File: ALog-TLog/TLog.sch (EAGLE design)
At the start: 98 parts, among them IC1 ATMEGA644M, J6 5.5x2.1mm Barrel, Q5 MOSFET_PCH-IRLML2244, Q6 MOSFET_PCH-IRLML2244, Q7 MOSFET_PCH-IRLML2244, Q8 MOSFET-NCH-BSS138, Q9 MOSFET-NCH-BSS138, U2 FT231X-Q, U3 915MHz, U4 SX1509, X2 87832-14

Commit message: Updated Gerber
Made changes to silk screen on universal header and updated gerber files
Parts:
- X2: device con-molex:87832-14 -> bschulz:87832-14
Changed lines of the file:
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@@
 <attribute name="MPN" value="RC0603FR-07330RL"/>
 </part>
-<part name="X2" library="con-molex" library_urn="urn:adsk.eagle:library:165" deviceset="87832-14" device="">
+<part name="X2" library="bschulz" deviceset="87832-14" device="">
 <attribute name="DIGIKEY" value="WM18702-ND"/>
 <attribute name="MF" value="Molex"/>

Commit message: Minor changes, updated gerber (presumptive final)
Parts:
- U$1: value CRYSTALTXC_8MHZ -> CRYSTAL_5X3.2_2LEAD; device bschulz:CRYSTALTXC_8MHZ -> bschulz:CRYSTAL_5X3.2_2LEAD
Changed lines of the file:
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@@
 <?xml version="1.0" encoding="utf-8"?>
 <!DOCTYPE eagle SYSTEM "eagle.dtd">
-<eagle version="8.5.1">
+<eagle version="8.3.2">
 <drawing>
 <settings>
@@
 <grid distance="0.1" unitdist="inch" unit="inch" style="lines" multiple="1" display="no" altdistance="0.01" altunitdist="inch" altunit="inch"/>
 <layers>
-<layer number="1" name="Top" color="4" fill="1" visible="yes" active="no"/>
-<layer number="2" name="Route2" color="1" fill="3" visible="yes" active="no"/>
-<layer number="3" name="Route3" color="4" fill="3" visible="yes" active="no"/>
-<layer number="4" name="Route4" color="1" fill="4" visible="yes" active="no"/>
-<layer number="5" name="Route5" color="4" fill="4" visible="yes" active="no"/>
-<layer number="6" name="Route6" color="1" fill="8" visible="yes" active="no"/>
-<layer number="7" name="Route7" color="4" fill="8" visible="yes" active="no"/>
-<layer number="8" name="Route8" color="1" fill="2" visible="yes" active="no"/>
-<layer number="9" name="Route9" color="4" fill="2" visible="yes" active="no"/>
-<layer number="10" name="Route10" color="1" fill="7" visible="yes" active="no"/>
-<layer number="11" name="Route11" color="4" fill="7" visible="yes" active="no"/>
-<layer number="12" name="Route12" color="1" fill="5" visible="yes" active="no"/>
-<layer number="13" name="Route13" color="4" fill="5" visible="yes" active="no"/>
-<layer number="14" name="Route14" color="1" fill="6" visible="yes" active="no"/>
-<layer number="15" name="Route15" color="4" fill="6" visible="yes" active="no"/>
-<layer number="16" name="Bottom" color="1" fill="1" visible="yes" active="no"/>
-<layer number="17" name="Pads" color="2" fill="1" visible="yes" active="no"/>
-<layer number="18" name="Vias" color="2" fill="1" visible="yes" active="no"/>
-<layer number="19" name="Unrouted" color="6" fill="1" visible="yes" active="no"/>
-<layer number="20" name="Dimension" color="15" fill="1" visible="yes" active="no"/>
-<layer number="21" name="tPlace" color="7" fill="1" visible="yes" active="no"/>
-<layer number="22" name="bPlace" color="7" fill="1" visible="yes" active="no"/>
-<layer number="23" name="tOrigins" color="15" fill="1" visible="yes" active="no"/>
-<layer number="24" name="bOrigins" color="15" fill="1" visible="yes" active="no"/>
-<layer number="25" name="tNames" color="7" fill="1" visible="yes" active="no"/>
-<layer number="26" name="bNames" color="7" fill="1" visible="yes" active="no"/>
-<layer number="27" name="tValues" color="7" fill="1" visible="yes" active="no"/>
-<layer number="28" name="bValues" color="7" fill="1" visible="yes" active="no"/>
+<layer number="1" name="Top" color="4" fill="1" visible="no" active="no"/>
+<layer number="2" name="Route2" color="1" fill="3" visible="no" active="no"/>
+<layer number="3" name="Route3" color="4" fill="3" visible="no" active="no"/>
+<layer number="4" name="Route4" color="1" fill="4" visible="no" active="no"/>
+<layer number="5" name="Route5" color="4" fill="4" visible="no" active="no"/>
+<layer number="6" name="Route6" color="1" fill="8" visible="no" active="no"/>
+<layer number="7" name="Route7" color="4" fill="8" visible="no" active="no"/>
+<layer number="8" name="Route8" color="1" fill="2" visible="no" active="no"/>
+<layer number="9" name="Route9" color="4" fill="2" visible="no" active="no"/>
+<layer number="10" name="Route10" color="1" fill="7" visible="no" active="no"/>
+<layer number="11" name="Route11" color="4" fill="7" visible="no" active="no"/>
+<layer number="12" name="Route12" color="1" fill="5" visible="no" active="no"/>
+<layer number="13" name="Route13" color="4" fill="5" visible="no" active="no"/>
+<layer number="14" name="Route14" color="1" fill="6" visible="no" active="no"/>
+<layer number="15" name="Route15" color="4" fill="6" visible="no" active="no"/>
+<layer number="16" name="Bottom" color="1" fill="1" visible="no" active="no"/>
+<layer number="17" name="Pads" color="2" fill="1" visible="no" active="no"/>
+<layer number="18" name="Vias" color="2" fill="1" visible="no" active="no"/>
+<layer number="19" name="Unrouted" color="6" fill="1" visible="no" active="no"/>
+<layer number="20" name="Dimension" color="15" fill="1" visible="no" active="no"/>
+<layer number="21" name="tPlace" color="7" fill="1" visible="no" active="no"/>
+<layer number="22" name="bPlace" color="7" fill="1" visible="no" active="no"/>
+<layer number="23" name="tOrigins" color="15" fill="1" visible="no" active="no"/>
+<layer number="24" name="bOrigins" color="15" fill="1" visible="no" active="no"/>
+<layer number="25" name="tNames" color="7" fill="1" visible="no" active="no"/>
+<layer number="26" name="bNames" color="7" fill="1" visible="no" active="no"/>
+<layer number="27" name="tValues" color="7" fill="1" visible="no" active="no"/>
+<layer number="28" name="bValues" color="7" fill="1" visible="no" active="no"/>
 <layer number="29" name="tStop" color="7" fill="3" visible="no" active="no"/>
 <layer number="30" name="bStop" color="7" fill="6" visible="no" active="no"/>
@@
 <layer number="35" name="tGlue" color="7" fill="4" visible="no" active="no"/>
 <layer number="36" name="bGlue" color="7" fill="5" visible="no" active="no"/>
-<layer number="37" name="tTest" color="7" fill="1" visible="yes" active="no"/>
-<layer number="38" name="bTest" color="7" fill="1" visible="yes" active="no"/>
+<layer number="37" name="tTest" color="7" fill="1" visible="no" active="no"/>
+<layer number="38" name="bTest" color="7" fill="1" visible="no" active="no"/>
 <layer number="39" name="tKeepout" color="4" fill="11" visible="no" active="no"/>
 <layer number="40" name="bKeepout" color="1" fill="11" visible="no" active="no"/>
@@
 <layer number="44" name="Drills" color="7" fill="1" visible="no" active="no"/>
 <layer number="45" name="Holes" color="7" fill="1" visible="no" active="no"/>
-<layer number="46" name="Milling" color="3" fill="1" visible="yes" active="no"/>
-<layer number="47" name="Measures" color="7" fill="1" visible="yes" active="no"/>
-<layer number="48" name="Document" color="7" fill="1" visible="yes" active="no"/>
-<layer number="49" name="Reference" color="7" fill="1" visible="yes" active="no"/>
-<layer number="50" name="dxf" color="7" fill="1" visible="yes" active="no"/>
-<layer number="51" name="tDocu" color="7" fill="1" visible="yes" active="no"/>
-<layer number="52" name="bDocu" color="7" fill="1" visible="yes" active="no"/>
-<layer number="53" name="tGND_GNDA" color="7" fill="9" visible="yes" active="no"/>
-<layer number="54" name="bGND_GNDA" color="1" fill="9" visible="yes" active="no"/>
-<layer number="56" name="wert" color="7" fill="1" visible="yes" active="no"/>
-<layer number="57" name="tCAD" color="7" fill="1" visible="yes" active="no"/>
-<layer number="59" name="tCarbon" color="7" fill="1" visible="yes" active="no"/>
-<layer number="60" name="bCarbon" color="7" fill="1" visible="yes" active="no"/>
+<layer number="46" name="Milling" color="3" fill="1" visible="no" active="no"/>
+<layer number="47" name="Measures" color="7" fill="1" visible="no" active="no"/>
+<layer number="48" name="Document" color="7" fill="1" visible="no" active="no"/>
+<layer number="49" name="Reference" color="7" fill="1" visible="no" active="no"/>
+<layer number="50" name="dxf" color="7" fill="1" visible="no" active="no"/>
+<layer number="51" name="tDocu" color="7" fill="1" visible="no" active="no"/>
+<layer number="52" name="bDocu" color="7" fill="1" visible="no" active="no"/>
+<layer number="53" name="tGND_GNDA" color="7" fill="9" visible="no" active="no"/>
+<layer number="54" name="bGND_GNDA" color="1" fill="9" visible="no" active="no"/>
+<layer number="56" name="wert" color="7" fill="1" visible="no" active="no"/>
+<layer number="57" name="tCAD" color="7" fill="1" visible="no" active="no"/>
+<layer number="59" name="tCarbon" color="7" fill="1" visible="no" active="no"/>
+<layer number="60" name="bCarbon" color="7" fill="1" visible="no" active="no"/>
 <layer number="90" name="Modules" color="5" fill="1" visible="yes" active="yes"/>
 <layer number="91" name="Nets" color="2" fill="1" visible="yes" active="yes"/>
@@
 <part name="U3" library="SparkFun-RF" library_urn="urn:adsk.eagle:library:531" deviceset="RFM69H" device="CW-915" value="915MHz"/>
 <part name="X1" library="bschulz" deviceset="SMA" device="_EDGE"/>
-<part name="R16" library="rcl" deviceset="R-EU_" device="R0603" value="FB">
+<part name="R16" library="rcl" library_urn="urn:adsk.eagle:library:334" deviceset="R-EU_" device="R0603" package3d_urn="urn:adsk.eagle:package:23555/2" value="FB">
 <attribute name="DIGIKEY" value="1276-6358-1-ND"/>
 <attribute name="MF" value="Samsung"/>
 <attribute name="MPN" value="CIC10P471NC"/>
 </part>
-<part name="R17" library="rcl" deviceset="R-EU_" device="R0603" value="FB">
+<part name="R17" library="rcl" library_urn="urn:adsk.eagle:library:334" deviceset="R-EU_" device="R0603" package3d_urn="urn:adsk.eagle:package:23555/2" value="FB">
 <attribute name="DIGIKEY" value="1276-6358-1-ND"/>
 <attribute name="MF" value="Samsung"/>
@@
 <part name="SUPPLY47" library="supply2" library_urn="urn:adsk.eagle:library:372" deviceset="GND" device=""/>
 <part name="MICRO_USB" library="bschulz" deviceset="MICRO_USB_LONGPADS" device=""/>
-<part name="U$1" library="bschulz" deviceset="CRYSTAL" device="TXC_8MHZ"/>
+<part name="U$1" library="bschulz" deviceset="CRYSTAL_5X3.2_2LEAD" device=""/>
 <part name="R4" library="bschulz" deviceset="R-EU_" device="R0603" technology="330" value="330">
 <attribute name="MPN" value="RC0603FR-07330RL"/>
@@
 will not be understood (or retained) with this version.
 </note>
+<note version="8.3" severity="warning">
+Since Version 8.3, EAGLE supports the association of 3D packages
+with devices in libraries, schematics, and board files. Those 3D
+packages will not be understood (or retained) with this version.
+</note>
 </compatibility>

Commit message: Presumptive Final gerbers for TLog Mrk 1.1
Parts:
- ISP2: device adafruit:AVRISP-6 -> bschulz:AVRISP-6
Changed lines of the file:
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@@
 <?xml version="1.0" encoding="utf-8"?>
 <!DOCTYPE eagle SYSTEM "eagle.dtd">
-<eagle version="8.3.2">
+<eagle version="8.5.1">
 <drawing>
 <settings>
@@
 <attribute name="MPN" value="OSTTE100104"/>
 </part>
-<part name="ISP2" library="adafruit" library_urn="urn:adsk.eagle:library:420" deviceset="AVRISP" device="-6">
+<part name="ISP2" library="bschulz" deviceset="AVRISP" device="-6">
 <attribute name="DIGIKEY" value="609-3234-ND"/>
 <attribute name="MF" value="Amphenol"/>

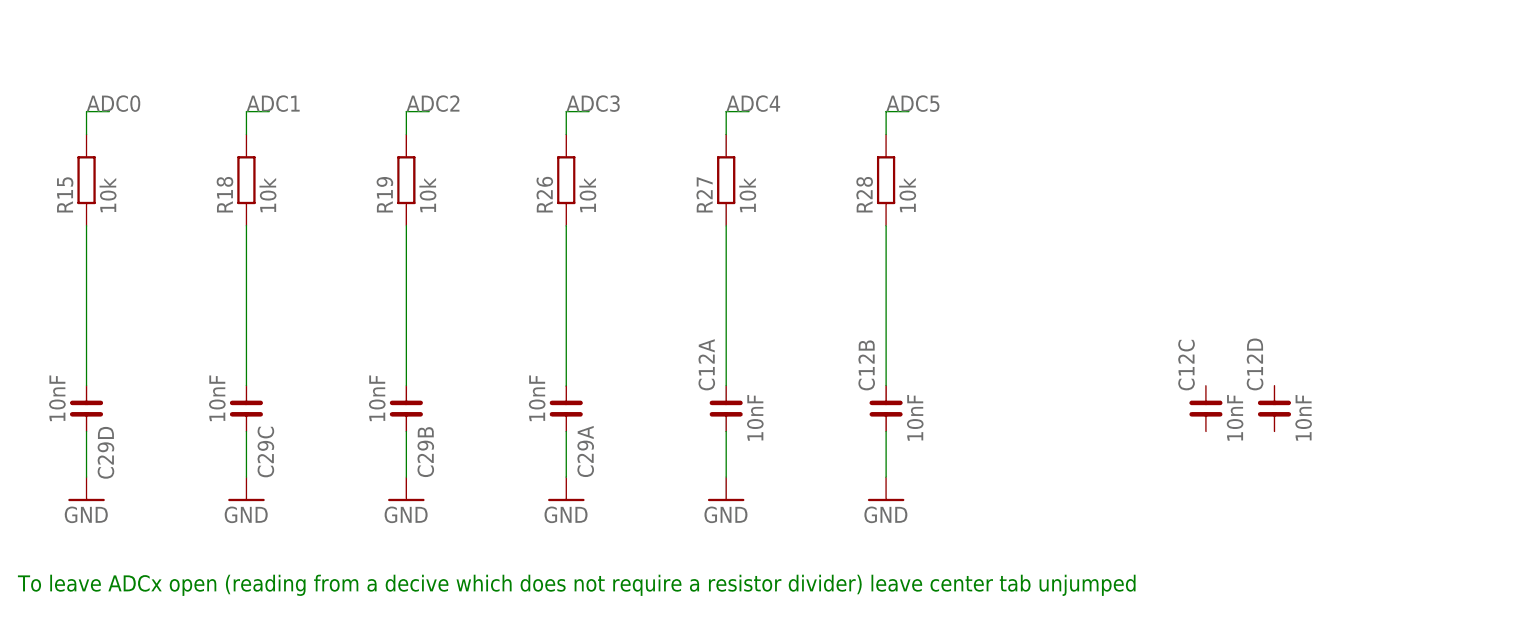
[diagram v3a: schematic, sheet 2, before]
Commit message: Issue Fix
Patial fix of issues: #12, #9, #8 (fixed in schematic, but not fully routed)
Full fix of issues: #10, #7
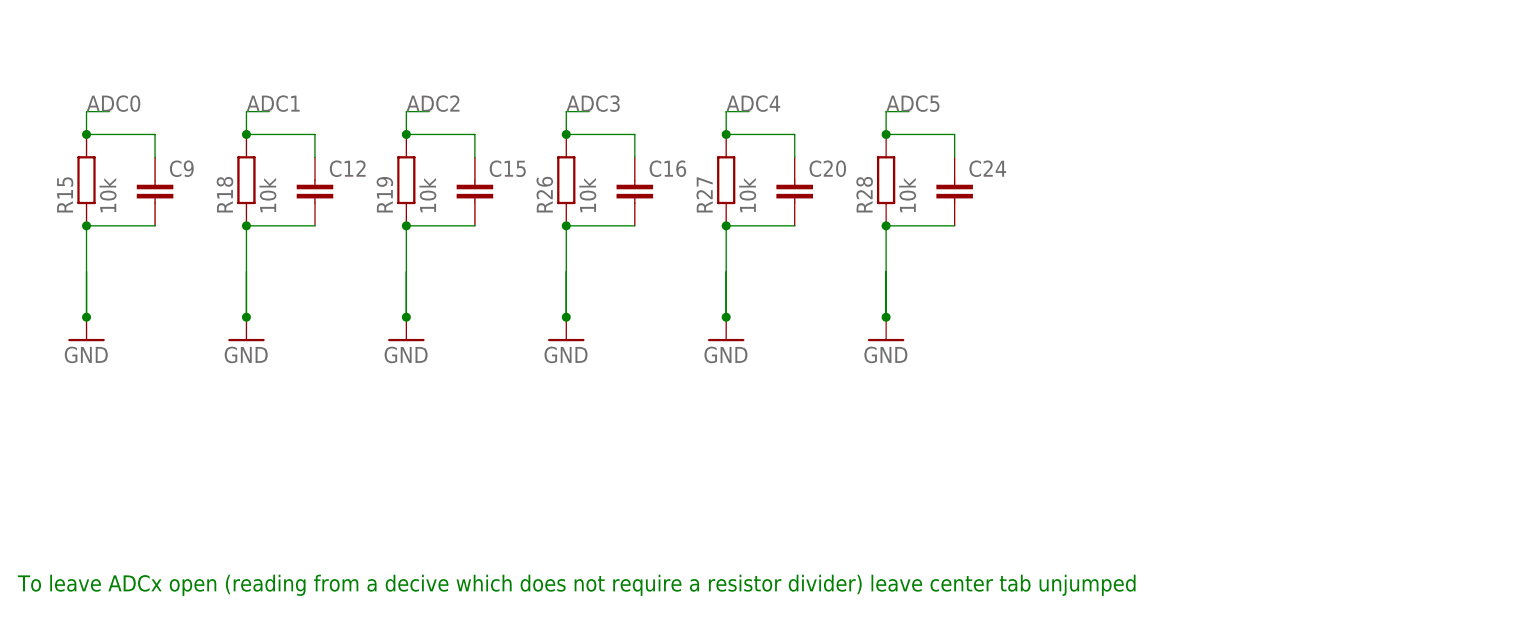
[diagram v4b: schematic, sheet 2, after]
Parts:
- removed C29: 10nF, rc-master-smd:CCA_ECJ-1206
- added C15, C16, C20, C24, C9: (no value), bschulz_passives:C-EUC0603
- added Q11: MOSFET-NCH-BSS138, bschulz:MOSFET-NCH-BSS138
- added Q12: MOSFET_PCH-IRLML2244, bschulz:MOSFET_PCH-IRLML2244
- added R20: 180k, bschulz_passives:R-EU_R0603
- added R21, R22: 10k, rcl:R-EU_R0603
- C12: value 10nF -> (none); device rc-master-smd:CCA_ECJ-1206 -> bschulz_passives:C-EUC0603; DIGIKEY 445-1854-1-ND -> (none); MF TDK -> (none); MPN CKCA43X7R1H103M100AA -> (none)
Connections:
- removed net N$17: C12B.2, R28.1
- removed net N$19: C29B.1, R19.1
- removed net N$24: C29A.1, R26.1
- removed net N$44: C29D.1, R15.1
- removed net N$45: C29C.1, R18.1
- removed net N$48: C12A.2, R27.1
- new net 5V_EXT: R25.2
- new net N$34: Q11.D, Q12.G, R21.2
- new net VUSB: C13.1, C17.1, MICRO_USB.VDD, Q11.G, Q12.D, R22.2
- net 3V3: now also R20.2; no longer C8.1, RTC1.VCC
- net 5V: now also Q12.S, R21.1; no longer C13.1, C17.1, MICRO_USB.VDD, R25.2
- net ADC0: now also C9.1
- net ADC1: now also C12.1
- net ADC2: now also C15.1
- net ADC3: now also C16.1
- net ADC4: now also C20.1
- net ADC5: now also C24.1
- net EXT_3.3V: now also C8.1, RTC1.VCC
- net GND: now also C12.2, C15.2, C16.2, C20.2, C24.2, C9.2, Q11.S, R15.1, R18.1, R19.1, R22.1, R26.1, R27.1, R28.1; no longer C12A.1, C12B.1, C29A.2, C29B.2, C29C.2, C29D.2
- net REF_CTRL: now also R20.1
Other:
- note removed: "NOTE: Add bi-directional converters for 5v I2C rail"
- note removed: "NOTE: Get info from Ying!"
- note removed: "NOTE: Verify connector!"
- note removed: "NOTE: Verify how to get full range operation!"
- note removed: "USB Programmer"
